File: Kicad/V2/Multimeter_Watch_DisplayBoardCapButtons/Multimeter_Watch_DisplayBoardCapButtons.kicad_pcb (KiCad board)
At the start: 2 copper layers, 46 x 42 mm, 10 parts, among them J1 51281-1294, U1 AT42QT1070-S

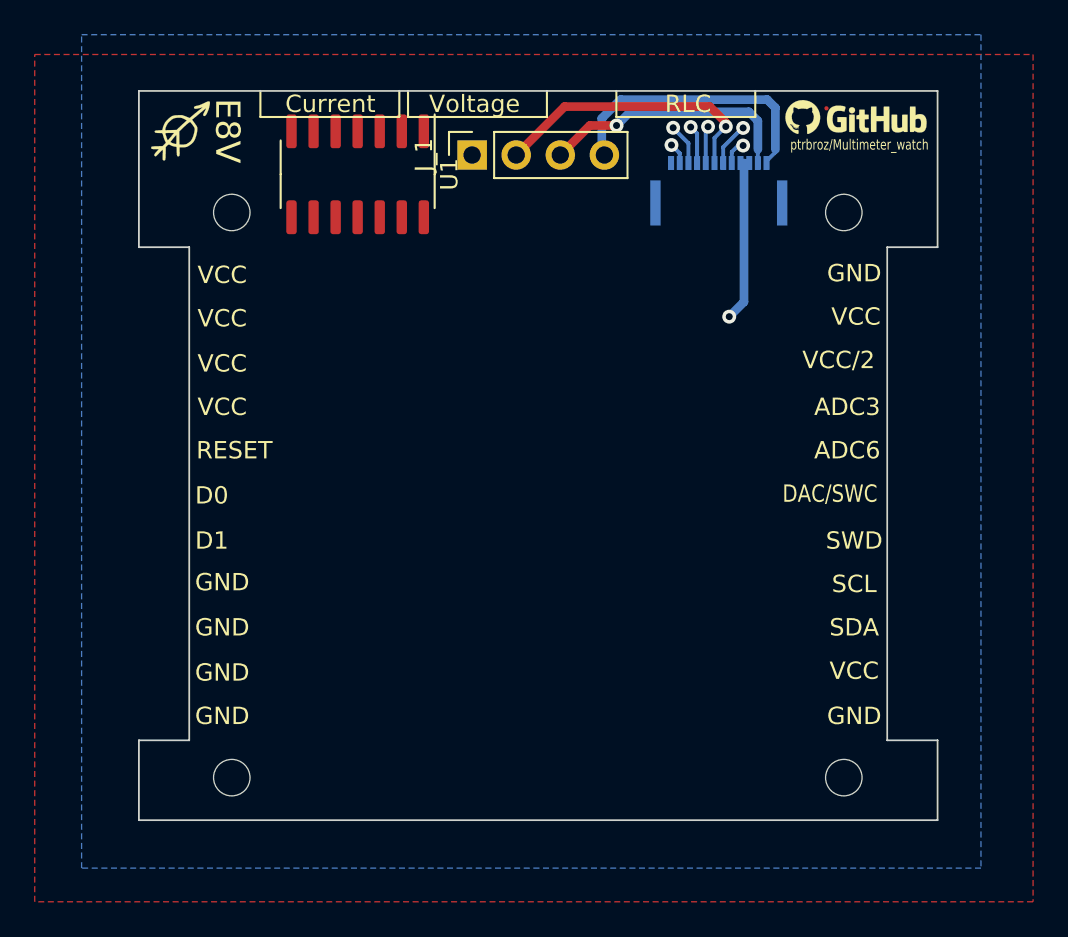
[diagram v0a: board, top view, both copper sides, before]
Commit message: top board capacitance buttons
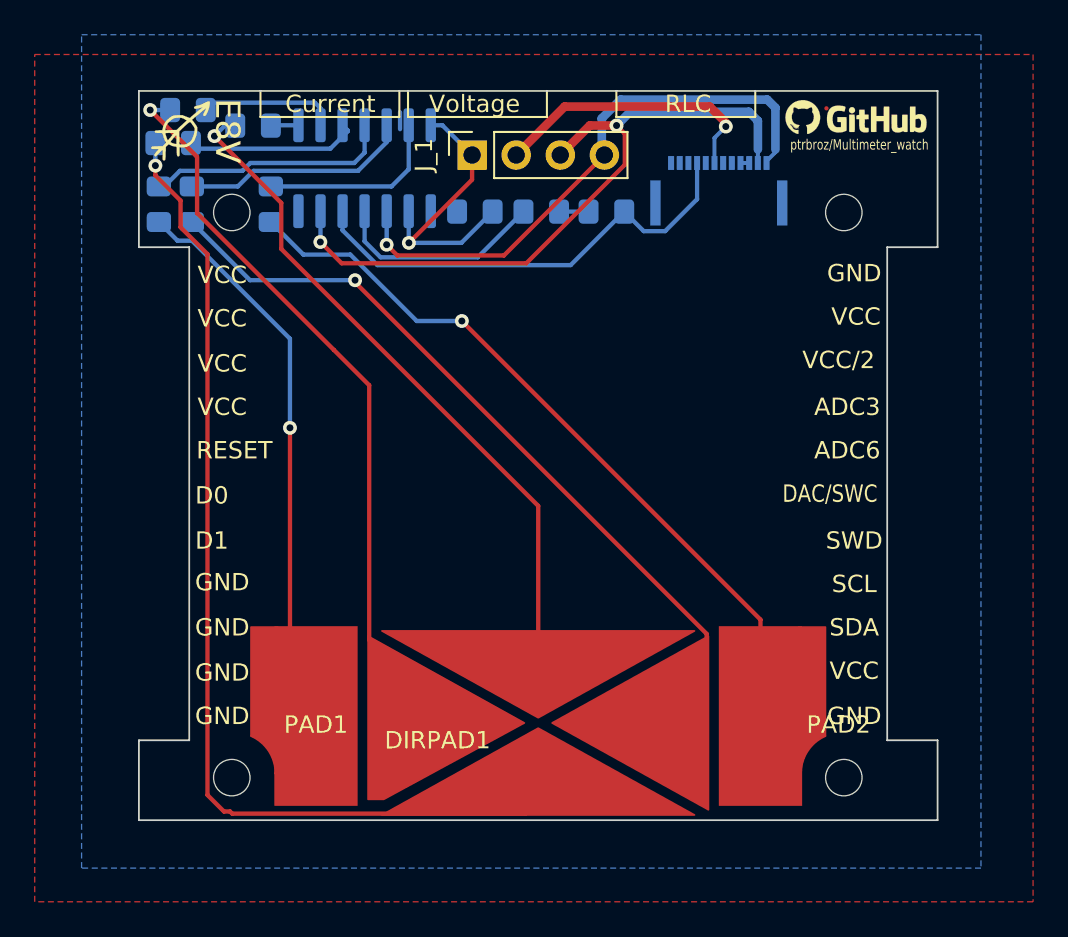
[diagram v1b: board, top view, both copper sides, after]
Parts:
- added C1: C_Small, Capacitor_SMD:C_0805_2012Metric_Pad1.15x1.40mm_HandSolder, B.Cu at (121.3, 65.0)
- added DIRPAD1: CapButtons_Directional, Multimeter_Watch_Custom_Footprints:CapButtons_Directional, F.Cu at (125.0, 94.4)
- added PAD1: Touch_Pad, Multimeter_Watch_Custom_Footprints:CapButton_Left, F.Cu at (112.2, 94.0)
- added PAD2: Touch_Pad, Multimeter_Watch_Custom_Footprints:CapButton_Right, F.Cu at (137.8, 94.0)
- added R1: R, Resistor_SMD:R_0805_2012Metric_Pad1.15x1.40mm_HandSolder, B.Cu at (128.9, 65.0)
- added R2: R, Resistor_SMD:R_0805_2012Metric_Pad1.15x1.40mm_HandSolder, B.Cu at (125.2, 65.0)
- added R3: R, Resistor_SMD:R_0805_2012Metric_Pad1.15x1.40mm_HandSolder, B.Cu at (109.6, 64.5)
- added R4: R, Resistor_SMD:R_0805_2012Metric_Pad1.15x1.40mm_HandSolder, B.Cu at (105.0, 64.5)
- added R5: R, Resistor_SMD:R_0805_2012Metric_Pad1.15x1.40mm_HandSolder, B.Cu at (103.2, 64.5)
- added R6: R, Resistor_SMD:R_0805_2012Metric_Pad1.15x1.40mm_HandSolder, B.Cu at (104.0, 61.0)
- added R7: R, Resistor_SMD:R_0805_2012Metric_Pad1.15x1.40mm_HandSolder, B.Cu at (104.8, 59.1)
- added R8: R, Resistor_SMD:R_0805_2012Metric_Pad1.15x1.40mm_HandSolder, B.Cu at (108.6, 60.0)
- U1: moved to B.Cu
- moved U1 0.53 mm to (115.0, 62.5), turned to 90 degrees
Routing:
- net Net-(DIRPAD1-Pad4): track 0.00 -> 59.8 mm, vias 0 -> 1
- net Net-(DIRPAD1-Pad1): track 0.00 -> 46.8 mm, vias 0 -> 1
- net Net-(DIRPAD1-Pad2): track 0.00 -> 45.0 mm, vias 0 -> 1
- net Net-(PAD2-Pad1): track 0.00 -> 43.2 mm, vias 0 -> 1
- net Net-(DIRPAD1-Pad3): track 0.00 -> 38.5 mm, vias 0 -> 1
- net Net-(PAD1-Pad1): track 0.00 -> 32.7 mm, vias 0 -> 1
- net /PB6: track 2.22 -> 26.9 mm, vias 1 -> 0
- net /SCL: track 15.1 -> 39.7 mm, vias 1 -> 2
- net /SDA: track 16.2 -> 33.3 mm, vias 0 -> 1
- net Net-(R5-Pad2): track 0.00 -> 14.2 mm
- net Net-(R4-Pad2): track 0.00 -> 13.3 mm
- net Net-(R2-Pad2): track 0.00 -> 12.4 mm
- net Net-(R3-Pad2): track 0.00 -> 11.9 mm
- net Net-(R6-Pad2): track 0.00 -> 10.1 mm
- net Net-(R7-Pad2): track 0.00 -> 7.90 mm
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
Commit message: minor changes to capbuttons board (??)
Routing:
- net /VCC: track 1.70 -> 20.1 mm
- net /GND: track 17.6 -> 23.4 mm, vias 1 -> 2
- net /SCL: track 39.7 -> 37.2 mm
- net Net-(DIRPAD1-Pad4): track 59.8 -> 58.5 mm
- net /PB5: track 16.0 -> 17.0 mm
